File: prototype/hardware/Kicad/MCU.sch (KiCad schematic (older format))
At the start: 9 parts

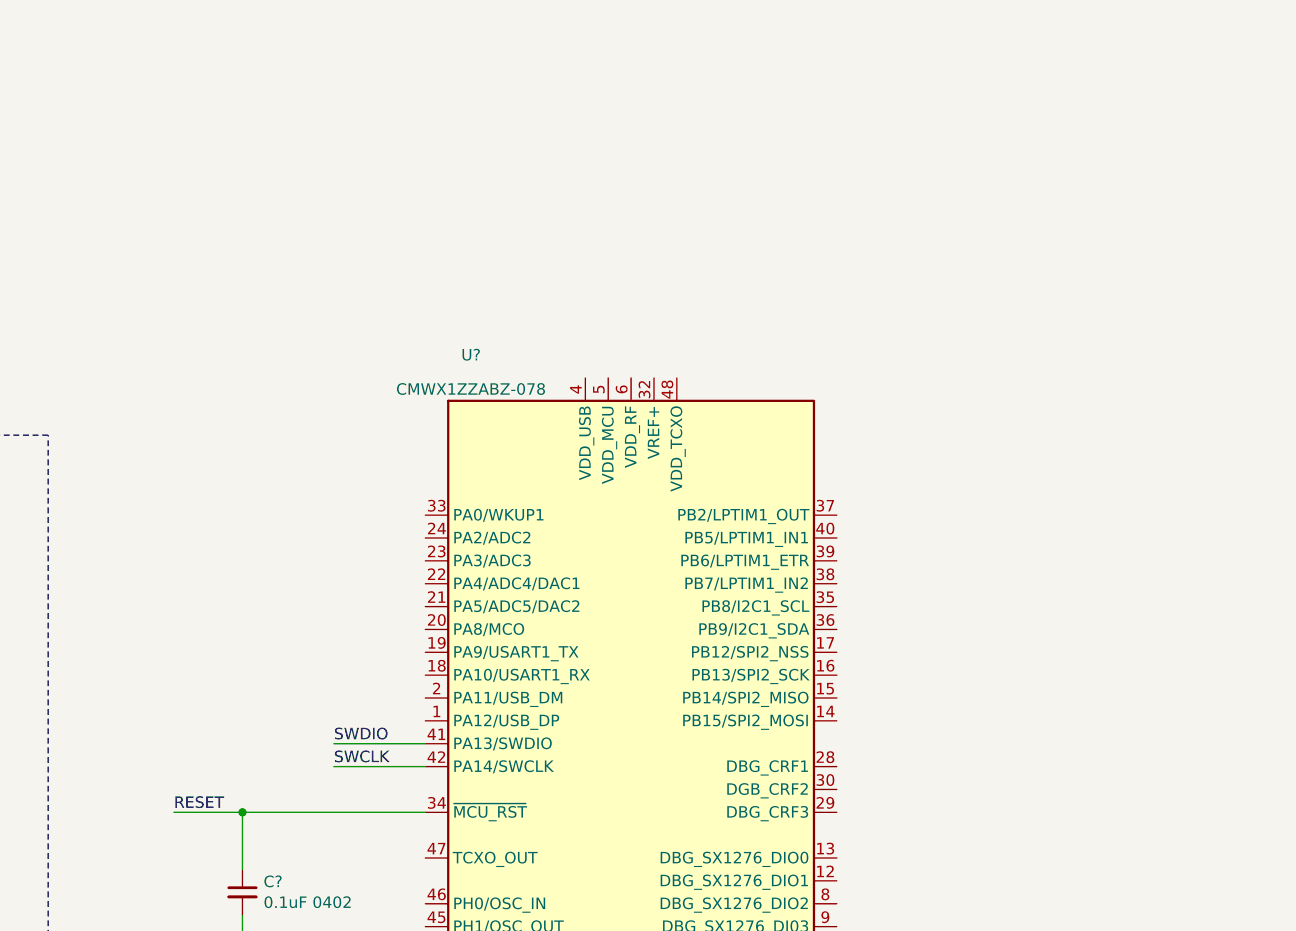
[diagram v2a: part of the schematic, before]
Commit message: setup power connections to mcu
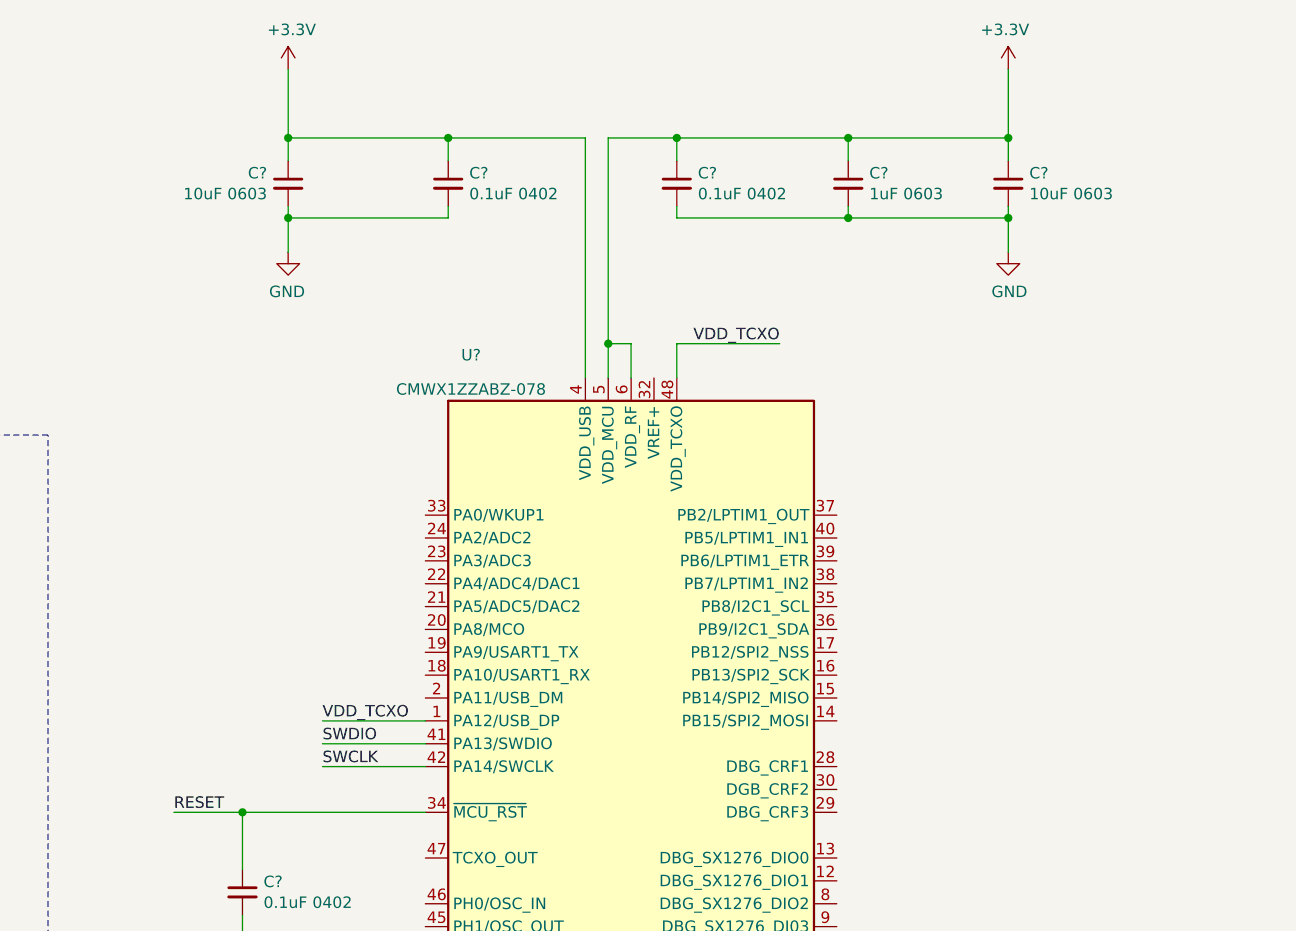
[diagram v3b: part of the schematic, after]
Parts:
- added C? (x2): 0.1uF 0402, symbol Device:C_Small
- added C?: 1uF 0603, symbol Device:C_Small
- added C? (x2): 10uF 0603, symbol Device:C_Small
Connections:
- net +3V3: now also U?.4 (VDD_USB), U?.5 (VDD_MCU), U?.6 (VDD_RF), C?.1, C?.1, C?.1, C?.1, C?.1
- net GND: now also C?.2, C?.2, C?.2, C?.2, C?.2
- net VDD_TCXO: now reaches U?.1 (PA12/USB_DP)
- net VDD_TCXO: now also U?.48 (VDD_TCXO)
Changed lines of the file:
@@
 $EndComp
 Wire Wire Line
-	4350 3700 3950 3700
-Text Label 3950 3700 0    50   ~ 0
+	4350 3700 3900 3700
+Text Label 3900 3700 0    50   ~ 0
 SWDIO
 Wire Wire Line
@@
 	1950 3650 2250 3650
 NoConn ~ 1950 3850
-Text Label 3950 3800 0    50   ~ 0
+Text Label 3900 3800 0    50   ~ 0
 SWCLK
 Wire Wire Line
-	3950 3800 4350 3800
+	3900 3800 4350 3800
 Text Label 2250 3450 2    50   ~ 0
 SWCLK
@@
 Wire Wire Line
 	3550 4450 3550 4600
+Wire Wire Line
+	5150 1050 5150 1950
+Wire Wire Line
+	5250 2100 5250 1950
+Wire Wire Line
+	5250 1950 5150 1950
+Connection ~ 5150 1950
+Wire Wire Line
+	5150 1950 5150 2100
+Wire Wire Line
+	5150 1050 5450 1050
+Wire Wire Line
+	5450 1050 5450 1150
+Wire Wire Line
+	5450 1400 6200 1400
+Connection ~ 5450 1050
+Wire Wire Line
+	5450 1050 6200 1050
+Wire Wire Line
+	6200 1050 6200 1150
+$Comp
+L Device:C_Small C?
+U 1 1 5DB8BFB9
+P 5450 1250
+F 0 "C?" H 5542 1296 50  0000 L CNN
+F 1 "0.1uF 0402" H 5542 1205 50  0000 L CNN
+F 2 "" H 5450 1250 50  0001 C CNN
+F 3 "~" H 5450 1250 50  0001 C CNN
+	1    5450 1250
+	1    0    0    -1
+$EndComp
+Wire Wire Line
+	5450 1350 5450 1400
+Connection ~ 6200 1050
+Connection ~ 6200 1400
+Wire Wire Line
+	6200 1400 6900 1400
+Wire Wire Line
+	6200 1050 6900 1050
+Connection ~ 6900 1050
+Wire Wire Line
+	6900 1050 6900 1150
+$Comp
+L power:+3.3V #PWR?
+U 1 1 5DB859BD
+P 6900 750
+F 0 "#PWR?" H 6900 600 50  0001 C CNN
+F 1 "+3.3V" H 6915 923 50  0000 C CNN
+F 2 "" H 6900 750 50  0001 C CNN
+F 3 "" H 6900 750 50  0001 C CNN
+	1    6900 750
+	-1   0    0    -1
+$EndComp
+Wire Wire Line
+	6900 1050 6900 750
+$Comp
+L Device:C_Small C?
+U 1 1 5DB9BD21
+P 6200 1250
+F 0 "C?" H 6292 1296 50  0000 L CNN
+F 1 "1uF 0603" H 6292 1205 50  0000 L CNN
+F 2 "" H 6200 1250 50  0001 C CNN
+F 3 "~" H 6200 1250 50  0001 C CNN
+	1    6200 1250
+	1    0    0    -1
+$EndComp
+Wire Wire Line
+	6200 1350 6200 1400
+$Comp
+L Device:C_Small C?
+U 1 1 5DB9C1FF
+P 6900 1250
+F 0 "C?" H 6992 1296 50  0000 L CNN
+F 1 "10uF 0603" H 6992 1205 50  0000 L CNN
+F 2 "" H 6900 1250 50  0001 C CNN
+F 3 "~" H 6900 1250 50  0001 C CNN
+	1    6900 1250
+	1    0    0    -1
+$EndComp
+Wire Wire Line
+	6900 1350 6900 1400
+$Comp
+L power:GND #PWR?
+U 1 1 5DB9DE92
+P 6900 1550
+F 0 "#PWR?" H 6900 1300 50  0001 C CNN
+F 1 "GND" H 6905 1377 50  0000 C CNN
+F 2 "" H 6900 1550 50  0001 C CNN
+F 3 "" H 6900 1550 50  0001 C CNN
+	1    6900 1550
+	1    0    0    -1
+$EndComp
+Wire Wire Line
+	6900 1550 6900 1400
+Connection ~ 6900 1400
+Wire Wire Line
+	4450 1050 4450 1150
+Connection ~ 4450 1050
+Wire Wire Line
+	4450 1400 3750 1400
+Wire Wire Line
+	4450 1050 3750 1050
+Connection ~ 3750 1050
+Wire Wire Line
+	3750 1050 3750 1150
+$Comp
+L power:+3.3V #PWR?
+U 1 1 5DBA9BB5
+P 3750 750
+F 0 "#PWR?" H 3750 600 50  0001 C CNN
+F 1 "+3.3V" H 3765 923 50  0000 C CNN
+F 2 "" H 3750 750 50  0001 C CNN
+F 3 "" H 3750 750 50  0001 C CNN
+	1    3750 750
+	1    0    0    -1
+$EndComp
+Wire Wire Line
+	3750 1050 3750 750
+$Comp
+L Device:C_Small C?
+U 1 1 5DBA9BC0
+P 4450 1250
+F 0 "C?" H 4358 1296 50  0000 R CNN
+F 1 "0.1uF 0402" H 4358 1205 50  0000 R CNN
+F 2 "" H 4450 1250 50  0001 C CNN
+F 3 "~" H 4450 1250 50  0001 C CNN
+	1    4450 1250
+	-1   0    0    -1
+$EndComp
+Wire Wire Line
+	4450 1350 4450 1400
+$Comp
+L Device:C_Small C?
+U 1 1 5DBA9BCB
+P 3750 1250
+F 0 "C?" H 3842 1296 50  0000 L CNN
+F 1 "10uF 0603" H 3842 1205 50  0000 L CNN
+F 2 "" H 3750 1250 50  0001 C CNN
+F 3 "~" H 3750 1250 50  0001 C CNN
+	1    3750 1250
+	-1   0    0    -1
+$EndComp
+Wire Wire Line
+	3750 1350 3750 1400
+$Comp
+L power:GND #PWR?
+U 1 1 5DBA9BD6
+P 3750 1550
+F 0 "#PWR?" H 3750 1300 50  0001 C CNN
+F 1 "GND" H 3755 1377 50  0000 C CNN
+F 2 "" H 3750 1550 50  0001 C CNN
+F 3 "" H 3750 1550 50  0001 C CNN
+	1    3750 1550
+	-1   0    0    -1
+$EndComp
+Wire Wire Line
+	3750 1550 3750 1400
+Connection ~ 3750 1400
+Wire Wire Line
+	5050 1050 5050 2100
+Wire Wire Line
+	4450 1050 5050 1050
+Wire Wire Line
+	5450 2100 5450 1950
+Wire Wire Line
+	5450 1950 5900 1950
+Text Label 5900 1950 2    50   ~ 0
+VDD_TCXO
+Text Label 3900 3600 0    50   ~ 0
+VDD_TCXO
+Wire Wire Line
+	4350 3600 3900 3600
 $EndSCHEMATC

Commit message: set up antenna pi network
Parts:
- added C? (x2): NF 0603, symbol Device:C_Small
- added L?: NF 0603, symbol Device:L
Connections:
- net GND: now also C?.2, C?.2
- net at U?.26 (ANT): now also C?.1, L?.2; no longer J?.1 (In)
- new net: C?.1, J?.1 (In), L?.1
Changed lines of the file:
@@
 	5250 5450 5250 5100
 Wire Wire Line
-	6150 4900 7550 4900
+	6150 4900 6550 4900
 $Comp
 L Connector:Conn_Coaxial J?
@@
 Wire Wire Line
 	4350 3600 3900 3600
+Wire Wire Line
+	6550 4900 6550 5100
+Connection ~ 6550 4900
+Wire Wire Line
+	6550 4900 6700 4900
+$Comp
+L power:GND #PWR?
+U 1 1 5DBCE3C8
+P 6550 5450
+F 0 "#PWR?" H 6550 5200 50  0001 C CNN
+F 1 "GND" H 6555 5277 50  0000 C CNN
+F 2 "" H 6550 5450 50  0001 C CNN
+F 3 "" H 6550 5450 50  0001 C CNN
+	1    6550 5450
+	1    0    0    -1
+$EndComp
+Wire Wire Line
+	7100 4900 7100 5100
+$Comp
+L power:GND #PWR?
+U 1 1 5DBCEFC5
+P 7100 5450
+F 0 "#PWR?" H 7100 5200 50  0001 C CNN
+F 1 "GND" H 7105 5277 50  0000 C CNN
+F 2 "" H 7100 5450 50  0001 C CNN
+F 3 "" H 7100 5450 50  0001 C CNN
+	1    7100 5450
+	1    0    0    -1
+$EndComp
+Connection ~ 7100 4900
+Wire Wire Line
+	7100 4900 7550 4900
+$Comp
+L Device:C_Small C?
+U 1 1 5DBD441B
+P 6550 5200
+F 0 "C?" H 6642 5246 50  0000 L CNN
+F 1 "NF 0603" H 6642 5155 50  0000 L CNN
+F 2 "" H 6550 5200 50  0001 C CNN
+F 3 "~" H 6550 5200 50  0001 C CNN
+	1    6550 5200
+	1    0    0    -1
+$EndComp
+Wire Wire Line
+	6550 5300 6550 5450
+$Comp
+L Device:C_Small C?
+U 1 1 5DBD4EF4
+P 7100 5200
+F 0 "C?" H 7192 5246 50  0000 L CNN
+F 1 "NF 0603" H 7192 5155 50  0000 L CNN
+F 2 "" H 7100 5200 50  0001 C CNN
+F 3 "~" H 7100 5200 50  0001 C CNN
+	1    7100 5200
+	1    0    0    -1
+$EndComp
+Wire Wire Line
+	7100 5300 7100 5450
+$Comp
+L Device:L L?
+U 1 1 5DBD576A
+P 6850 4900
+F 0 "L?" V 6669 4900 50  0000 C CNN
+F 1 "NF 0603" V 6760 4900 50  0000 C CNN
+F 2 "" H 6850 4900 50  0001 C CNN
+F 3 "~" H 6850 4900 50  0001 C CNN
+	1    6850 4900
+	0    1    1    0
+$EndComp
+Wire Wire Line
+	7000 4900 7100 4900
 $EndSCHEMATC
